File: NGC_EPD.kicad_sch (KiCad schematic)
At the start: 36 parts, among them J1 Conn_ARM_JTAG_SWD_10, J2 EPD_FCC, Q1 NMOS, U1 NGC1081, U2 TPS62125DSG

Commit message: Added boost,assigned footprints. Antenna pending
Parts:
- added AE1: Antenna_Loop, symbol Device:Antenna_Loop
- added C17: 1mF, Capacitor_THT:CP_Radial_D5.0mm_P2.00mm, symbol Device:C_Small
- added C18, C19: 1uF, Capacitor_SMD:C_0805_2012Metric_Pad1.18x1.45mm_HandSolder, symbol Device:C_Small
- added D4: D_Schottky_Small, Package_TO_SOT_SMD:SOT-23-3, symbol Device:D_Schottky_Small
- added D5: D_Zener_Small, Package_TO_SOT_SMD:SOT-23-3, symbol Device:D_Zener_Small
- added L3: 100uH, Inductor_SMD:L_1008_2520Metric_Pad1.43x2.20mm_HandSolder, symbol Device:L_Small
- added Q2: NMOS, Package_TO_SOT_SMD:SOT-23-3, symbol Simulation_SPICE:NMOS
- added R10: 10, Resistor_SMD:R_0402_1005Metric, symbol Device:R_Small
- added R9: 100K, Resistor_SMD:R_0805_2012Metric_Pad1.20x1.40mm_HandSolder, symbol Device:R_Small
- C1: footprint Capacitor_SMD:C_0805_2012Metric -> Capacitor_SMD:C_0805_2012Metric_Pad1.18x1.45mm_HandSolder
- C10, C11, C12, C13, C14, C5, C6, C7, C8, C9: footprint (none) -> Capacitor_SMD:C_0805_2012Metric_Pad1.18x1.45mm_HandSolder
- C15, C16: footprint Capacitor_THT:CP_Radial_D5.0mm_P2.00mm -> Capacitor_SMD:C_0805_2012Metric_Pad1.18x1.45mm_HandSolder
- C3: value 1uF -> 2uF; footprint Capacitor_SMD:C_0805_2012Metric -> Capacitor_SMD:C_0805_2012Metric_Pad1.18x1.45mm_HandSolder
- D1, D2, D3, Q1: footprint (none) -> Package_TO_SOT_SMD:SOT-23-3
- J2: footprint (none) -> Connector_FFC-FPC:TE_2-1734839-4_1x24-1MP_P0.5mm_Horizontal
- JP2: footprint (none) -> Connector_PinHeader_2.54mm:PinHeader_1x03_P2.54mm_Vertical
- L1, L2: footprint (none) -> Inductor_SMD:L_1008_2520Metric_Pad1.43x2.20mm_HandSolder
- R1, R2, R3: footprint Resistor_SMD:R_0402_1005Metric -> Resistor_SMD:R_0805_2012Metric_Pad1.20x1.40mm_HandSolder
- R4: footprint (none) -> Resistor_SMD:R_0402_1005Metric_Pad0.72x0.64mm_HandSolder
- R5, R6, R7, R8: footprint (none) -> Resistor_SMD:R_0805_2012Metric_Pad1.20x1.40mm_HandSolder
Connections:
- net BOOST_OUT: now also C4.1, D4.1 (K), D5.1 (K)
- net BOOST_PWM: now also R10.1
- net GND: now also C4.2, C17.2, D5.2 (A), Q2.3 (S), R9.2
- net VCC_HB: now also C17.1, L3.1
- net at U1.18 (LA): now also AE1.2, C18.1, C19.1
- net at U1.19 (LB): now also AE1.1, C18.2, C19.2
- new net: Q2.2 (G), R10.2, R9.1
- new net: D4.2 (A), L3.2, Q2.1 (D)
- no-connect marks 4 -> 20
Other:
- moved on the sheet: C3, C4, JP1, JP2

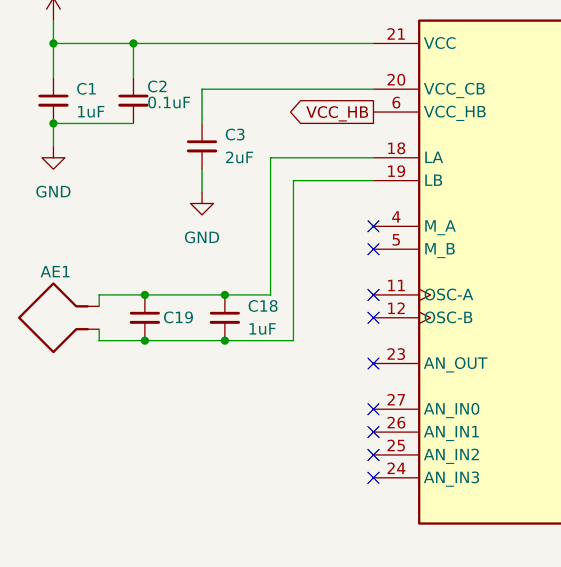
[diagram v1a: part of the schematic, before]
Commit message: Finished layout. Seperate antena board required.
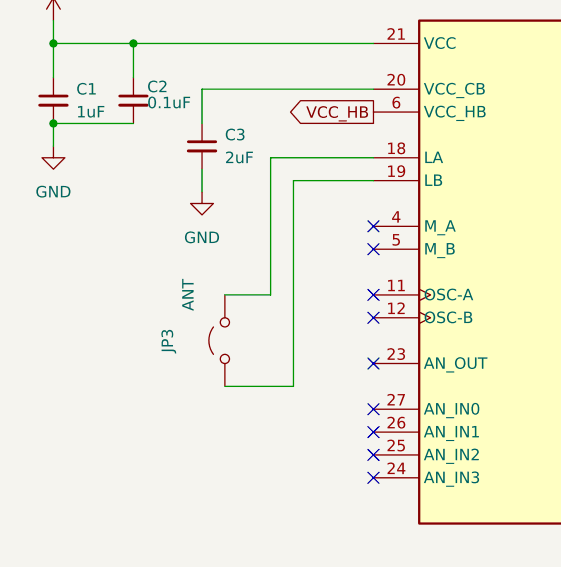
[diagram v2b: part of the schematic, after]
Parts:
- removed AE1: Antenna_Loop, symbol Device:Antenna_Loop
- removed C18, C19: 1uF, Capacitor_SMD:C_0805_2012Metric_Pad1.18x1.45mm_HandSolder, symbol Device:C_Small
- added JP3: ANT, Connector_PinHeader_2.54mm:PinHeader_2x01_P2.54mm_Vertical, symbol Jumper:Jumper_2_Open
- D1, D2, D3, D4, D5: footprint Package_TO_SOT_SMD:SOT-23-3 -> Diode_SMD:D_SOD-123
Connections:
- net at U1.18 (LA): now also JP3.2 (B)
- net at U1.19 (LB): now also JP3.1 (A)

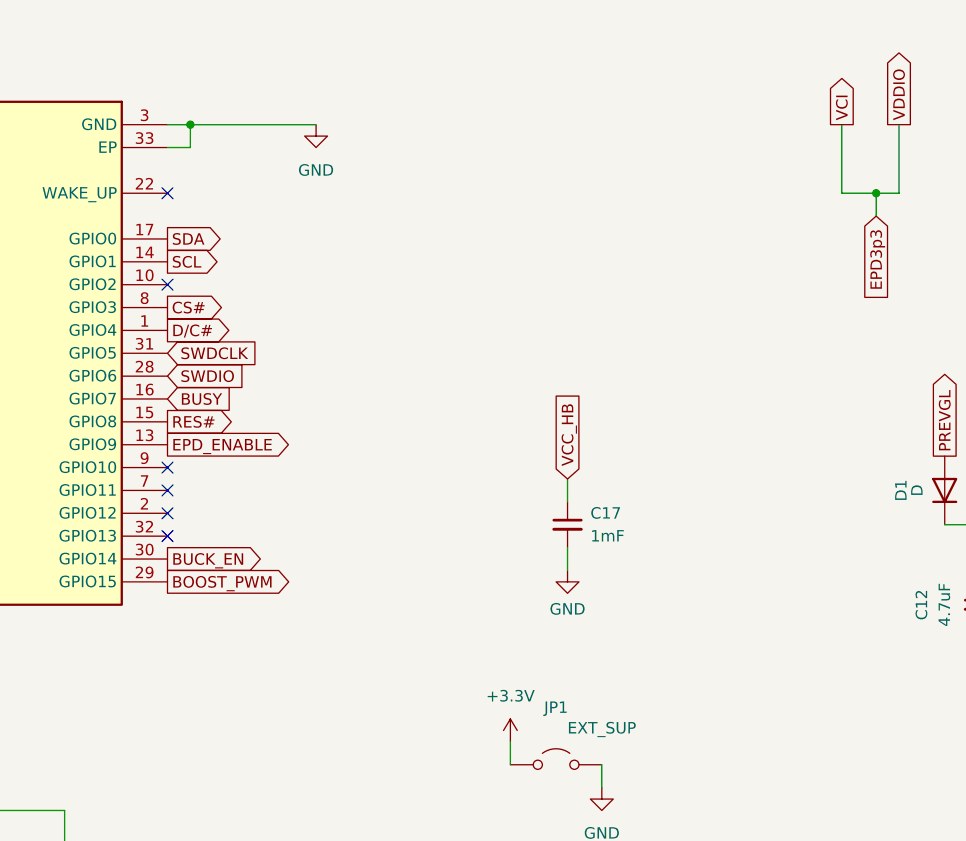
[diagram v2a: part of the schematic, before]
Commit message: Changed EPD FCC to backside. Added Testpoints and Infineon logo.
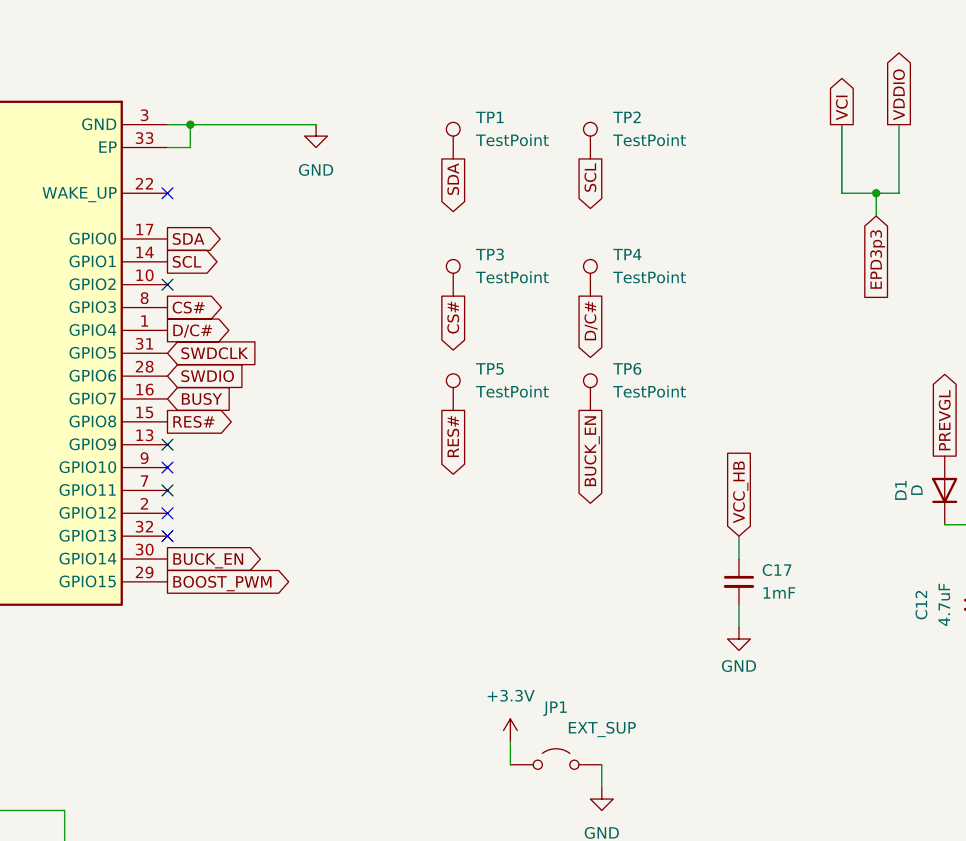
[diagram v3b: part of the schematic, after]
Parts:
- added TP1, TP2, TP3, TP4, TP5, TP6: TestPoint, TestPoint:TestPoint_Pad_1.0x1.0mm, symbol Connector:TestPoint
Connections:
- net BUCK_EN: now also TP6.1
- net CS#: now also TP3.1
- net D/C#: now also TP4.1
- net RES#: now also TP5.1
- net SCL: now also TP2.1
- net SDA: now also TP1.1
- net EPD_ENABLE: no longer names the net of U1.13 (GPIO9)
- no-connect marks 20 -> 21
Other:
- moved on the sheet: C17

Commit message: Complete fresh layout. Grouped a functional block components. Placed all the required test points and changed sizes of components (mostly to 0603). Created a single board including antenna(snapable). Created a new antenna design(Draw lines->align->Convert them to tracks) which satisfies the net list.
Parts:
- added C18: C_Tune, Capacitor_SMD:C_0603_1608Metric_Pad1.08x0.95mm_HandSolder, symbol Device:C_Small
- added JP4: EXT_SUP, Connector_PinHeader_2.54mm:PinHeader_1x02_P2.54mm_Vertical, symbol Jumper:Jumper_2_Open
- C1, C10, C11, C12, C13, C14, C15, C16, C3, C5, C6, C7, C8, C9: footprint Capacitor_SMD:C_0805_2012Metric_Pad1.18x1.45mm_HandSolder -> Capacitor_SMD:C_0603_1608Metric_Pad1.08x0.95mm_HandSolder
- C17: footprint Capacitor_THT:CP_Radial_D5.0mm_P2.00mm -> NGC_EPD_FootprintLib:1mF_Nichicon UVR0J102MPD
- C4: value 5mF -> 4.7mF; footprint Capacitor_THT:CP_Radial_D5.0mm_P2.00mm -> NGC_EPD_FootprintLib:CAP_PK&slash_PZ_12P5X25_LOW_RUB
- D4: value D_Schottky_Small -> D; symbol Device:D_Schottky_Small -> Device:D
- JP1: footprint Connector_PinHeader_2.54mm:PinHeader_2x01_P2.54mm_Vertical -> Connector_PinHeader_2.54mm:PinHeader_1x02_P2.54mm_Vertical
- JP2: now in the parts list
- JP3: value ANT -> EXT_SUP; footprint Connector_PinHeader_2.54mm:PinHeader_2x01_P2.54mm_Vertical -> Connector_PinHeader_2.54mm:PinHeader_1x02_P2.54mm_Vertical
- L1, L2: footprint Inductor_SMD:L_1008_2520Metric_Pad1.43x2.20mm_HandSolder -> Inductor_SMD:L_0603_1608Metric_Pad1.05x0.95mm_HandSolder
- L3: footprint Inductor_SMD:L_1008_2520Metric_Pad1.43x2.20mm_HandSolder -> Inductor_SMD:L_0805_2012Metric_Pad1.05x1.20mm_HandSolder
- Q1, Q2: footprint Package_TO_SOT_SMD:SOT-23-3 -> Package_TO_SOT_SMD:TSOT-23_HandSoldering
- R1, R2, R3, R5, R7, R8, R9: footprint Resistor_SMD:R_0805_2012Metric_Pad1.20x1.40mm_HandSolder -> Resistor_SMD:R_0603_1608Metric_Pad0.98x0.95mm_HandSolder
- R10: footprint Resistor_SMD:R_0402_1005Metric -> Resistor_SMD:R_0402_1005Metric_Pad0.72x0.64mm_HandSolder
- TP1, TP2, TP3, TP4, TP5, TP6: footprint TestPoint:TestPoint_Pad_1.0x1.0mm -> Connector_PinHeader_1.00mm:PinHeader_1x01_P1.00mm_Vertical
- U2: footprint Package_SON:WSON-8-1EP_2x2mm_P0.5mm_EP0.9x1.6mm_ThermalVias -> Package_SON:WSON-8-1EP_2x2mm_P0.5mm_EP0.9x1.6mm
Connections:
- net at JP3.2 (B), U1.18 (LA): now also JP3.1 (A), U1.19 (LB), C18.1, C18.2, JP4.1 (A), JP4.2 (B)
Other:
- moved on the sheet: D4
